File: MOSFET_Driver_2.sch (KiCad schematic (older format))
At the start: 20 parts, among them Q10 TPHR8504PL, Q11 TPHR8504PL, Q12 TPHR8504PL, Q7 TPHR8504PL, Q8 TPHR8504PL, Q9 TPHR8504PL, U1 FD6288Q

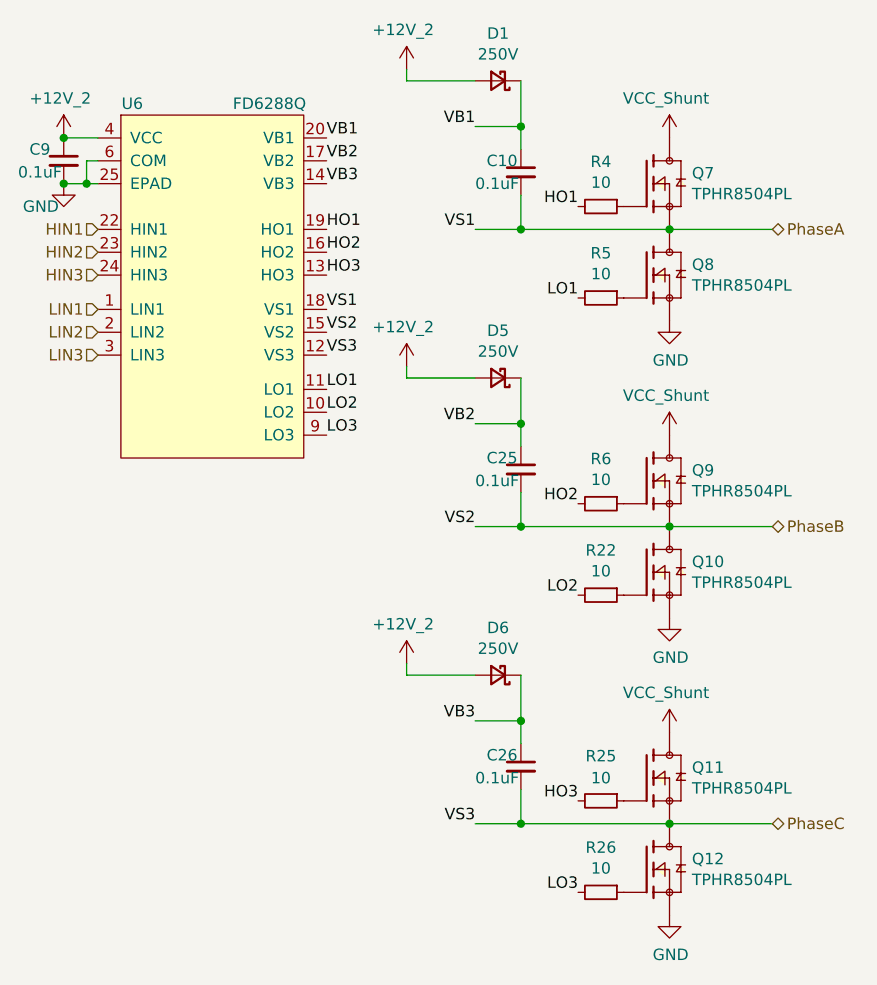
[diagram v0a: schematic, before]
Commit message: Lots of changes made with back being rerouted
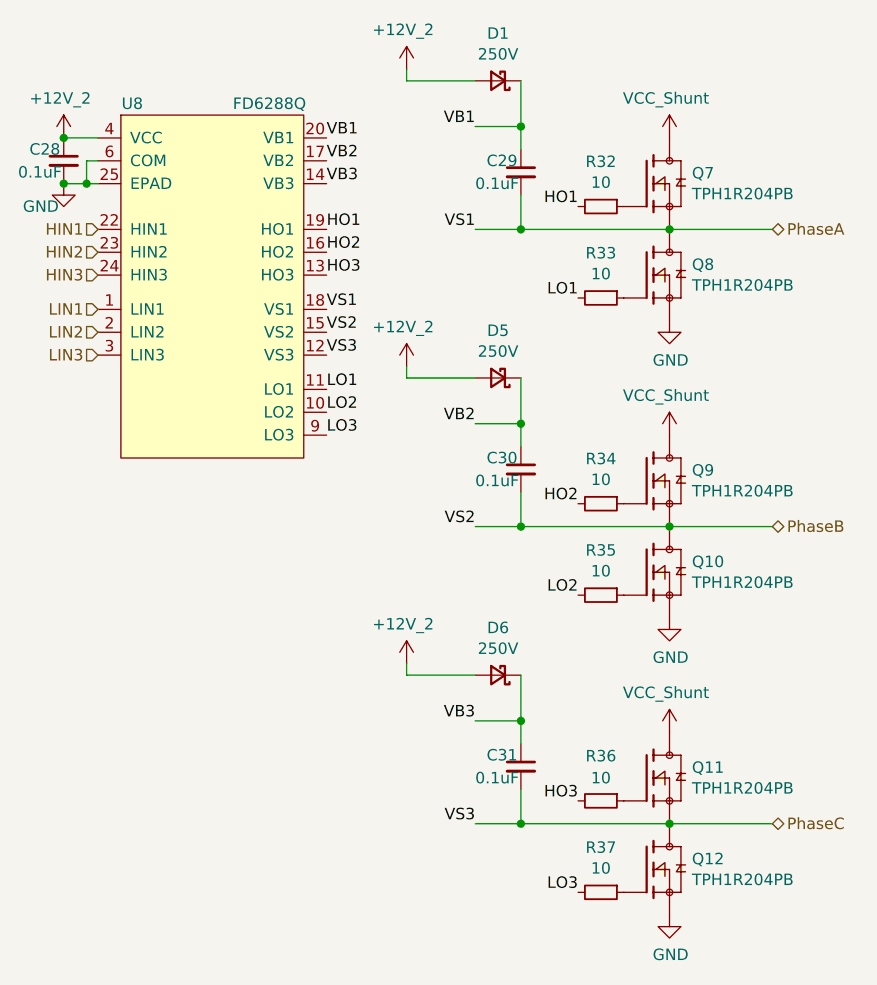
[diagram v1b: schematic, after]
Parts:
- removed Q10, Q11, Q12, Q7, Q8, Q9: TPHR8504PL, Footprints:TPHR8504PL, symbol JPW_Symbols:TPHR8504PL
- added Q10, Q11, Q12, Q7, Q8, Q9: TPH1R204PB, Footprints:TPH1R204PB, symbol JPW_Symbols:TPH1R204PB
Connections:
- net GND: now also Q10.1, Q10.2, Q10.3, Q12.1, Q12.2, Q12.3, Q8.1, Q8.2, Q8.3
- net PhaseA: now also Q7.1, Q7.2, Q7.3, Q8.5, Q8.6, Q8.7, Q8.8, Q8.9
- net PhaseB: now also Q10.5, Q10.6, Q10.7, Q10.8, Q10.9, Q9.1, Q9.2, Q9.3
- net PhaseC: now also Q11.1, Q11.2, Q11.3, Q12.5, Q12.6, Q12.7, Q12.8, Q12.9
- net VCC_Shunt: now also Q11.5, Q11.6, Q11.7, Q11.8, Q11.9, Q7.5, Q7.6, Q7.7, Q7.8, Q7.9, Q9.5, Q9.6, Q9.7, Q9.8, Q9.9
- net at R12.1: now also Q12.4
- net at R7.1: now also Q7.4
- net at R8.1: now also Q8.4
- net at R10.1: now also Q10.4
- net at R9.1: now also Q9.4
- net at R11.1: now also Q11.4
